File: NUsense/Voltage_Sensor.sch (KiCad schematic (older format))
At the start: 24 parts, among them U701 ACS724, U702 bq76920, U703 5_PIN_JST

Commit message: Cleans up some minor things
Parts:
- 0.1uF701: value 0.1nF -> 0n1F
- C701: renamed from C705; value C -> 6n8F
- renumbered C701 to C702, C702 to C703, C703 to C704, C704 to C705
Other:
- moved on the sheet: 0.1uF701, 1nF701, C701, C702, C703, C704, C705, C706, C707, C708, C709, C710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

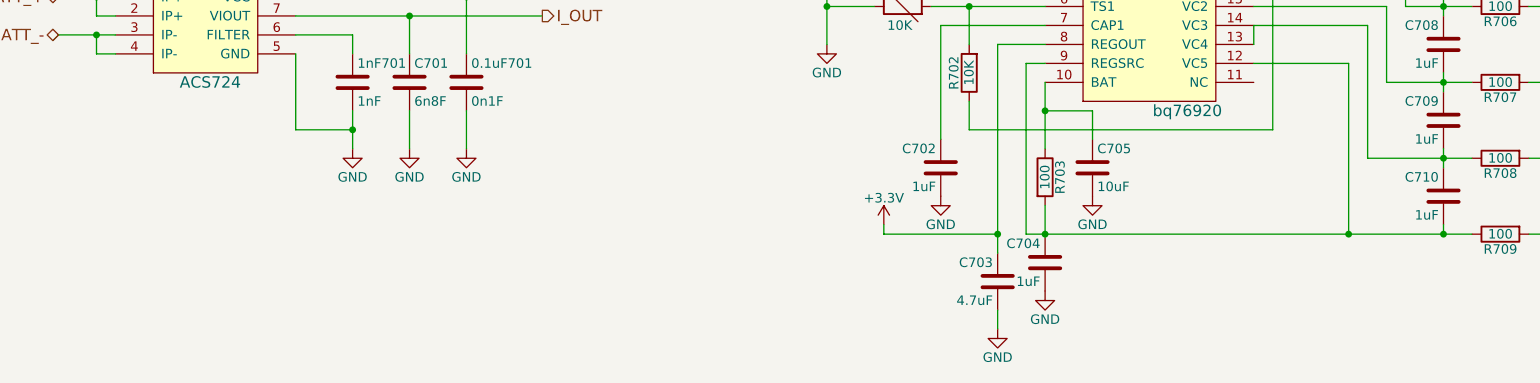
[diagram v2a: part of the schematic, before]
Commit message: Add labels
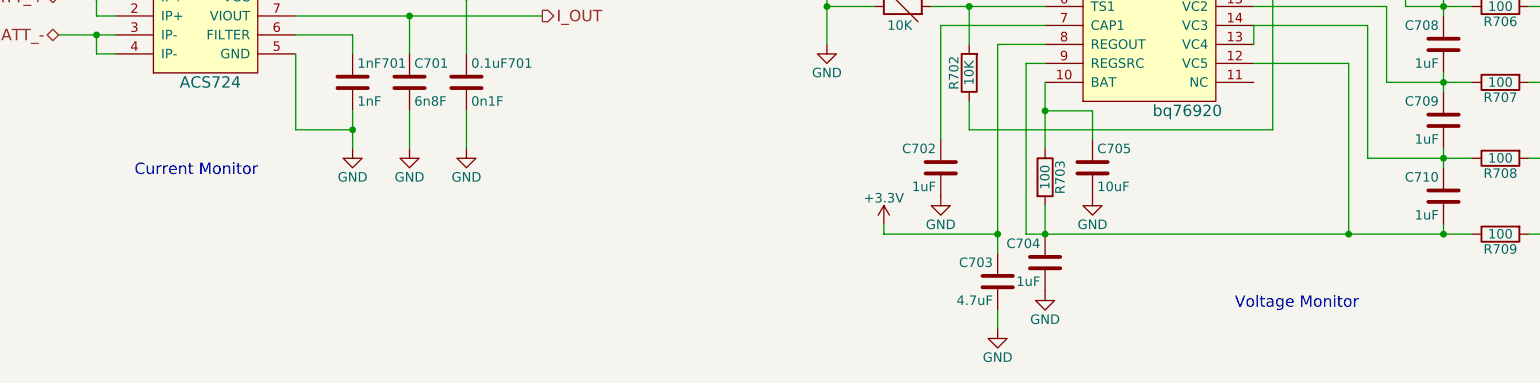
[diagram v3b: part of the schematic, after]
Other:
- note added: "Current Monitor"
- note added: "Voltage Monitor"
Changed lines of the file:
@@
 Wire Wire Line
 	5950 4400 5950 4450
+Text Notes 2000 4150 0    60   ~ 0
+Current Monitor
+Text Notes 7800 4850 0    60   ~ 0
+Voltage Monitor
 $EndSCHEMATC
